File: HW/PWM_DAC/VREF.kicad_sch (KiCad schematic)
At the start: 19 parts, among them Q1 2N7002, U1 ADR4550, U2 ADA4522-2

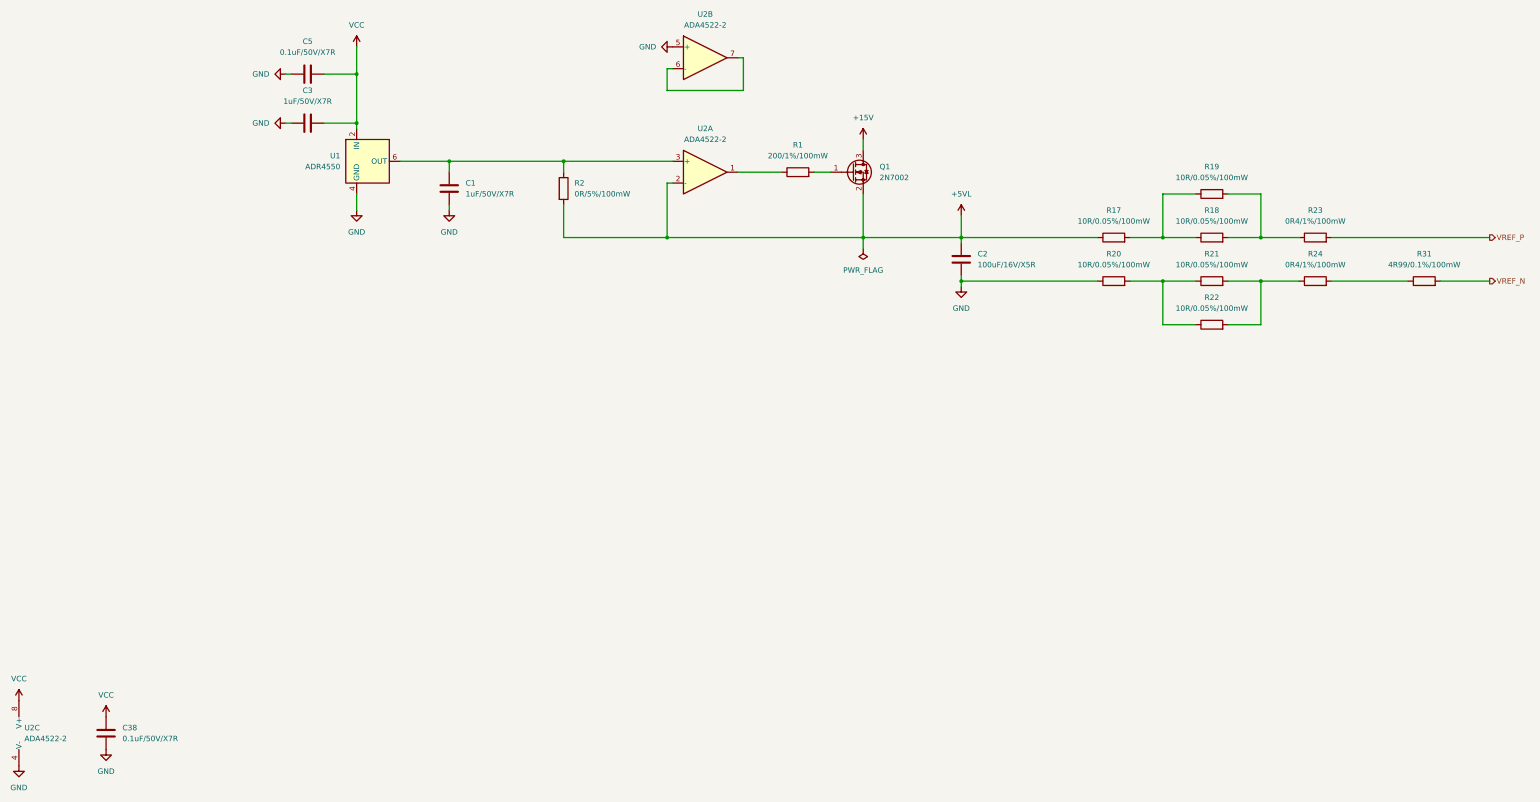
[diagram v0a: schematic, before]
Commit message: Schematic done
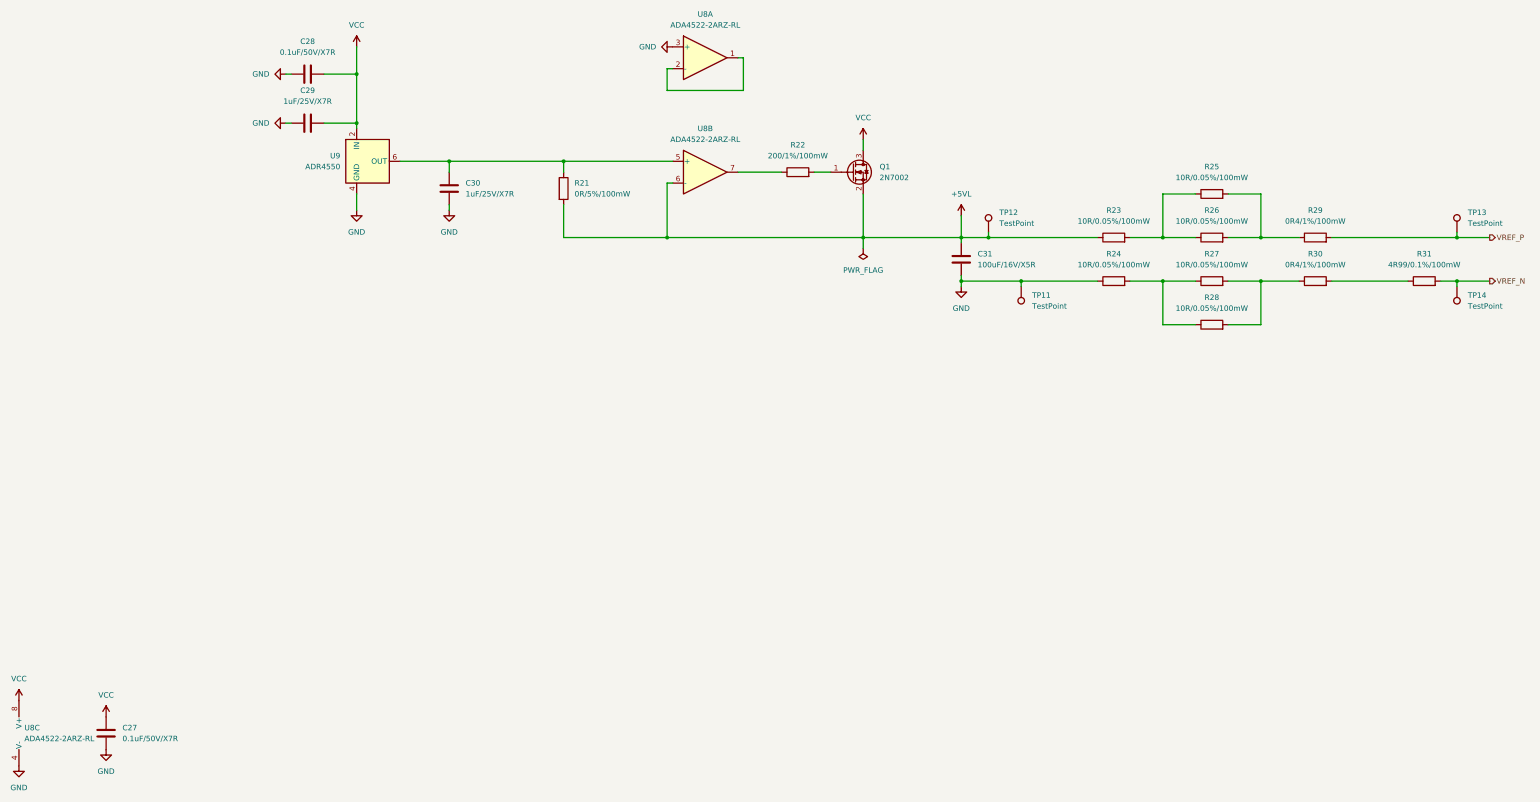
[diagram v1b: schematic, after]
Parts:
- added TP11, TP12, TP13, TP14: TestPoint, TestPoint:TestPoint_Pad_D1.5mm, symbol Connector:TestPoint
- C27: renamed from C38; footprint (none) -> Capacitor_SMD:C_0603_1608Metric_Pad1.08x0.95mm_HandSolder
- C28: renamed from C5; footprint (none) -> Capacitor_SMD:C_0603_1608Metric_Pad1.08x0.95mm_HandSolder
- C29: renamed from C3; value 1uF/50V/X7R -> 1uF/25V/X7R; footprint (none) -> Capacitor_SMD:C_0603_1608Metric_Pad1.08x0.95mm_HandSolder
- C30: renamed from C1; value 1uF/50V/X7R -> 1uF/25V/X7R; footprint (none) -> Capacitor_SMD:C_0603_1608Metric_Pad1.08x0.95mm_HandSolder
- C31: renamed from C2; footprint (none) -> Capacitor_SMD:C_1210_3225Metric_Pad1.33x2.70mm_HandSolder
- R21: renamed from R2; footprint (none) -> Resistor_SMD:R_0603_1608Metric_Pad0.98x0.95mm_HandSolder
- R22: renamed from R1; footprint (none) -> Resistor_SMD:R_0603_1608Metric_Pad0.98x0.95mm_HandSolder
- R23: renamed from R17; footprint (none) -> Resistor_SMD:R_0805_2012Metric_Pad1.20x1.40mm_HandSolder
- R24: renamed from R20; footprint (none) -> Resistor_SMD:R_0805_2012Metric_Pad1.20x1.40mm_HandSolder
- R25: renamed from R19; footprint (none) -> Resistor_SMD:R_0805_2012Metric_Pad1.20x1.40mm_HandSolder
- R26: renamed from R18; footprint (none) -> Resistor_SMD:R_0805_2012Metric_Pad1.20x1.40mm_HandSolder
- R27: renamed from R21; footprint (none) -> Resistor_SMD:R_0805_2012Metric_Pad1.20x1.40mm_HandSolder
- R28: renamed from R22; footprint (none) -> Resistor_SMD:R_0805_2012Metric_Pad1.20x1.40mm_HandSolder
- R29: renamed from R23; footprint (none) -> Resistor_SMD:R_0603_1608Metric_Pad0.98x0.95mm_HandSolder
- R30: renamed from R24; footprint (none) -> Resistor_SMD:R_0603_1608Metric_Pad0.98x0.95mm_HandSolder
- R31: footprint (none) -> Resistor_SMD:R_0805_2012Metric_Pad1.20x1.40mm_HandSolder
- U8: renamed from U2; value ADA4522-2 -> ADA4522-2ARZ-RL; footprint Module:Adafruit_Feather -> Package_SO:SOIC-8_3.9x4.9mm_P1.27mm
- renumbered U1 to U9
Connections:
- net +15V is gone; now on net VCC: Q1.3 (D)
- net +5VL: now also U8.6 (-), TP12.1; no longer U8.2 (-)
- net GND: now also U8.3 (+), TP11.1; no longer U8.5 (+)
- net VREF_N: now also TP14.1
- net VREF_P: now also TP13.1
- net at U8.1: now also U8.2 (-); no longer R22.1
- net at C30.1, R21.1, U9.6 (OUT): now also U8.5 (+); no longer U8.3 (+)
- net at U8.7: now also R22.1; no longer U8.6 (-)
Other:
- moved on the sheet: U8A, U8B

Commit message: Layout done
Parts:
- R21: now not fitted
- R29, R30: value 0R4/1%/100mW -> 0.4R/1%/100mW
- R31: value 4R99/0.1%/100mW -> 4.99R/0.1%/100mW
- U9: value ADR4550 -> ADR4550BRZ-R7
- renumbered TP12 to TP11, TP11 to TP12

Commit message: Layout
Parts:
- R21: now left out of the parts list
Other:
- moved on the sheet: C27
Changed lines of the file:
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@@
 	(symbol
 		(lib_id "power:VCC")
-		(at 49.53 259.08 0)
+		(at 54.61 259.08 0)
 		(unit 1)
 		(body_style 1)
@@
 		(fields_autoplaced yes)
 		(property "Reference" "#PWR063"
-			(at 49.53 262.89 0)
+			(at 54.61 262.89 0)
 			(hide yes)
 			(show_name no)
@@
 		)
 		(property "Value" "VCC"
-			(at 49.53 254 0)
+			(at 54.61 254 0)
 			(show_name no)
 			(do_not_autoplace no)
@@
 		)
 		(property "Footprint" "Package_QFP:TQFP-44_10x10mm_P0.8mm"
-			(at 49.53 259.08 0)
+			(at 54.61 259.08 0)
 			(hide yes)
 			(show_name no)
@@
 		)
 		(property "Datasheet" ""
-			(at 49.53 259.08 0)
+			(at 54.61 259.08 0)
 			(hide yes)
 			(show_name no)
@@
 		)
 		(property "Description" "Power symbol creates a global label with name \"VCC\""
-			(at 49.53 259.08 0)
+			(at 54.61 259.08 0)
 			(hide yes)
 			(show_name no)
@@
 	(symbol
 		(lib_id "power:GND")
-		(at 49.53 266.7 0)
+		(at 54.61 266.7 0)
 		(unit 1)
 		(body_style 1)
@@
 		(fields_autoplaced yes)
 		(property "Reference" "#PWR064"
-			(at 49.53 273.05 0)
+			(at 54.61 273.05 0)
 			(hide yes)
 			(show_name no)
@@
 		)
 		(property "Value" "GND"
-			(at 49.53 271.78 0)
+			(at 54.61 271.78 0)
 			(show_name no)
 			(do_not_autoplace no)
@@
 		)
 		(property "Footprint" ""
-			(at 49.53 266.7 0)
+			(at 54.61 266.7 0)
 			(hide yes)
 			(show_name no)
@@
 		)
 		(property "Datasheet" ""
-			(at 49.53 266.7 0)
+			(at 54.61 266.7 0)
 			(hide yes)
 			(show_name no)
@@
 		)
 		(property "Description" "Power symbol creates a global label with name \"GND\" , ground"
-			(at 49.53 266.7 0)
+			(at 54.61 266.7 0)
 			(hide yes)
 			(show_name no)
@@
 		(body_style 1)
 		(exclude_from_sim no)
-		(in_bom yes)
+		(in_bom no)
 		(on_board yes)
 		(in_pos_files yes)
@@
 	(symbol
 		(lib_id "Device:C")
-		(at 49.53 262.89 180)
+		(at 54.61 262.89 180)
 		(unit 1)
 		(body_style 1)
@@
 		(fields_autoplaced yes)
 		(property "Reference" "C27"
-			(at 53.34 261.6199 0)
+			(at 58.42 261.6199 0)
 			(show_name no)
 			(do_not_autoplace no)
@@
 		)
 		(property "Value" "0.1uF/50V/X7R"
-			(at 53.34 264.1599 0)
+			(at 58.42 264.1599 0)
 			(show_name no)
 			(do_not_autoplace no)
@@
 		)
 		(property "Footprint" "Capacitor_SMD:C_0603_1608Metric_Pad1.08x0.95mm_HandSolder"
-			(at 48.5648 259.08 0)
+			(at 53.6448 259.08 0)
 			(hide yes)
 			(show_name no)
@@
 		)
 		(property "Datasheet" ""
-			(at 49.53 262.89 0)
+			(at 54.61 262.89 0)
 			(hide yes)
 			(show_name no)
@@
 		)
 		(property "Description" "Unpolarized capacitor"
-			(at 49.53 262.89 0)
+			(at 54.61 262.89 0)
 			(hide yes)
 			(show_name no)
@@
 		)
 		(property "Sim.Device" ""
-			(at 49.53 262.89 0)
+			(at 54.61 262.89 0)
 			(hide yes)
 			(show_name no)
@@
 		)
 		(property "Sim.Pins" ""
-			(at 49.53 262.89 0)
-			(hide yes)
-			(show_name no)
+			(at 54.61 262.89 0)
+			(hide yes)
+			(show_name no)

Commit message: PCB files send
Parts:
- removed U9: ADR4550BRZ-R7, Package_SO:SOIC-8_3.9x4.9mm_P1.27mm, symbol Reference_Voltage:ADR4550
- added U9: LT1461CCS8-5#TRPBF, Package_SO:SOIC-8_3.9x4.9mm_P1.27mm, symbol Reference_Voltage:LT1461BxS8-5
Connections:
- net GND: now also U9.4 (GND)
- net VCC: now also U9.2 (VIN)
- net at C30.1, R21.1, U8.5 (+): now also U9.6 (VOUT)
- no-connect marks 0 -> 1
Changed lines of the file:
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@@
 		(color 0 0 0 0)
 	)
+	(no_connect
+		(at 97.79 129.54)
+	)
 	(wire
 		(pts
@@
 	)
 	(symbol
+		(lib_id "Reference_Voltage:LT1461BxS8-5")
+		(at 107.95 129.54 0)
+		(unit 1)
+		(body_style 1)
+		(exclude_from_sim no)
+		(in_bom yes)
+		(on_board yes)
+		(in_pos_files yes)
+		(dnp no)
+		(fields_autoplaced yes)
+		(property "Reference" "U9"
+			(at 128.27 123.1198 0)
+			(show_name no)
+			(do_not_autoplace no)
+			(effects
+				(font
+					(size 1.27 1.27)
+				)
+			)
+		)
+		(property "Value" "LT1461CCS8-5#TRPBF"
+			(at 128.27 125.6598 0)
+			(show_name no)
+			(do_not_autoplace no)
+			(effects
+				(font
+					(size 1.27 1.27)
+				)
+			)
+		)
+		(property "Footprint" "Package_SO:SOIC-8_3.9x4.9mm_P1.27mm"
+			(at 99.06 129.54 0)
+			(hide yes)
+			(show_name no)
+			(do_not_autoplace no)
+			(effects
+				(font
+					(size 1.27 1.27)
+				)
+			)
+		)
+		(property "Datasheet" "https://www.analog.com/media/en/technical-documentation/data-sheets/LT1461.pdf"
+			(at 99.06 129.54 0)
+			(hide yes)
+			(show_name no)
+			(do_not_autoplace no)
+			(effects
+				(font
+					(size 1.27 1.27)
+				)
+			)
+		)
+		(property "Description" "Voltage Reference, ±0.06%, 5V, 100mA, 5.5V-20V Vin, SOIC-8"
+			(at 107.95 129.54 0)
+			(hide yes)
+			(show_name no)
+			(do_not_autoplace no)
+			(effects
+				(font
+					(size 1.27 1.27)
+				)
+			)
+		)
+		(pin "1"
+		)
+		(pin "6"
+		)
+		(pin "3"
+		)
+		(pin "2"
+		)
+		(pin "7"
+		)
+		(pin "4"
+		)
+		(pin "8"
+		)
+		(pin "5"
+		)
+		(instances
+			(project "PWM_DAC"
+				(path "/2c9a3dd6-931b-4123-b00f-9baea7dc6b77/e2989761-872c-4e27-95c1-5b6d4b908eeb"
+					(reference "U9")
+					(unit 1)
+				)
+			)
+		)
+	)
+	(symbol
 		(lib_id "power:GND")
 		(at 91.44 120.65 270)
@@
 					(unit 1)
 				)
-			)
-		)
-	)
-	(symbol
-		(lib_id "Reference_Voltage:ADR4550")
-		(at 110.49 129.54 0)
-		(unit 1)
-		(body_style 1)
-		(exclude_from_sim no)
-		(in_bom yes)
-		(on_board yes)
-		(in_pos_files yes)
-		(dnp no)
-		(property "Reference" "U9"
-			(at 104.14 128.2699 0)
-			(show_name no)
-			(do_not_autoplace no)
-			(effects
-				(font
-					(size 1.27 1.27)
-				)
-				(justify right)
-			)
-		)
-		(property "Value" "ADR4550BRZ-R7"
-			(at 104.14 130.81 0)
-			(show_name no)
-			(do_not_autoplace no)
-			(effects
-				(font
-					(size 1.27 1.27)
-				)
-				(justify right)
-			)
-		)
-		(property "Footprint" "Package_SO:SOIC-8_3.9x4.9mm_P1.27mm"
-			(at 113.03 137.16 0)
-			(hide yes)
-			(show_name no)
-			(do_not_autoplace no)
-			(effects
-				(font
-					(size 1.27 1.27)
-					(italic yes)
-				)
-			)
-		)
-		(property "Datasheet" "https://www.analog.com/media/en/technical-documentation/data-sheets/ADR4520_4525_4530_4533_4540_4550.pdf"
-			(at 113.03 138.43 0)
-			(hide yes)
-			(show_name no)
-			(do_not_autoplace no)
-			(effects
-				(font
-					(size 1.27 1.27)
-					(italic yes)
-				)
-			)
-		)
-		(property "Description" "5.0V,  Ultralow Noise, High Accuracy Voltage Reference, SOIC-8"
-			(at 110.49 129.54 0)
-			(hide yes)
-			(show_name no)
-			(do_not_autoplace no)
-			(effects
-				(font
-					(size 1.27 1.27)
-				)
-			)
-		)
-		(property "Sim.Device" ""
-			(at 110.49 129.54 0)
-			(hide yes)
-			(show_name no)
-			(do_not_autoplace no)
-			(effects
-				(font
-					(size 1.27 1.27)
-				)
-			)
-		)
-		(property "Sim.Pins" ""
-			(at 110.49 129.54 0)
-			(hide yes)
-			(show_name no)
-			(do_not_autoplace no)
-			(effects
-				(font
-					(size 1.27 1.27)
-				)
-			)
-		)
-		(pin "8"
-		)
-		(pin "3"
-		)
-		(pin "7"
-		)
-		(pin "6"
-		)
-		(pin "5"
-		)
-		(pin "4"
-		)
-		(pin "2"
-		)
-		(pin "1"
-		)
-		(instances
-			(project "PWM_DAC"
-				(path "/2c9a3dd6-931b-4123-b00f-9baea7dc6b77/e2989761-872c-4e27-95c1-5b6d4b908eeb"
-					(reference "U9")
-					(unit 1)
-				)
